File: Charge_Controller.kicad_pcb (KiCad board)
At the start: 2 copper layers, 127 x 73.7 mm, 147 parts, among them J1 SOLAR, J10 Conn_01x01_Female, J11 Conn_01x01_Female, J12 Conn_01x01_Female, J13 Conn_01x01_Female, J14 Conn_01x01_Female, J15 Conn_01x01_Female, J16 Conn_01x01_Female, J17 Conn_01x01_Female, J18 Conn_01x01_Female, J19 Conn_01x01_Female, J2 Conn_01x01_Female, J20 Conn_01x01_Female, J21 Conn_01x01_Female, J22 Conn_01x01_Female, J23 Conn_01x01_Female, J24 Conn_01x01_Female, J25 Conn_01x01_Female, J26 Conn_01x01_Female, J27 Conn_01x01_Female, J28 Conn_01x01_Female, J29 Conn_01x01_Female, J3 Conn_01x01_Female, J30 Conn_01x01_Female, J31 Conn_01x01_Female, J32 Conn_01x01_Female, J33 SOLAR, J34 BATT, J35 BATT, J36 FAN, J37 I2C_CON, J38 I2C_CON, J4 Conn_01x01_Female, J5 Conn_01x01_Female, J6 Conn_01x01_Female, J7 Conn_01x01_Female, J8 BATT, J9 USB_OTG, Q1 CSD19505, Q2 CSD19505, Q3 CSD19505, Q4 Si2306, Q5 2N3904, Q6 2N3904, Q7 PMOS-100V-78A, Q8 PMOS-100V-78A, Q9 Si2306, SW1 RIGHT, SW2 RIGHT, SW3 RIGHT, SW4 RIGHT, U1 ACS712-30A, U10 ADS1015, U11 NUP4202, U2 B1212, U3 AMS1117-5.0, U4 AMS1117-3.3, U5 XL7005A, U6 XL7005A, U7 IR2104, U8 ESP32-WROOM-32, U9 CH340G

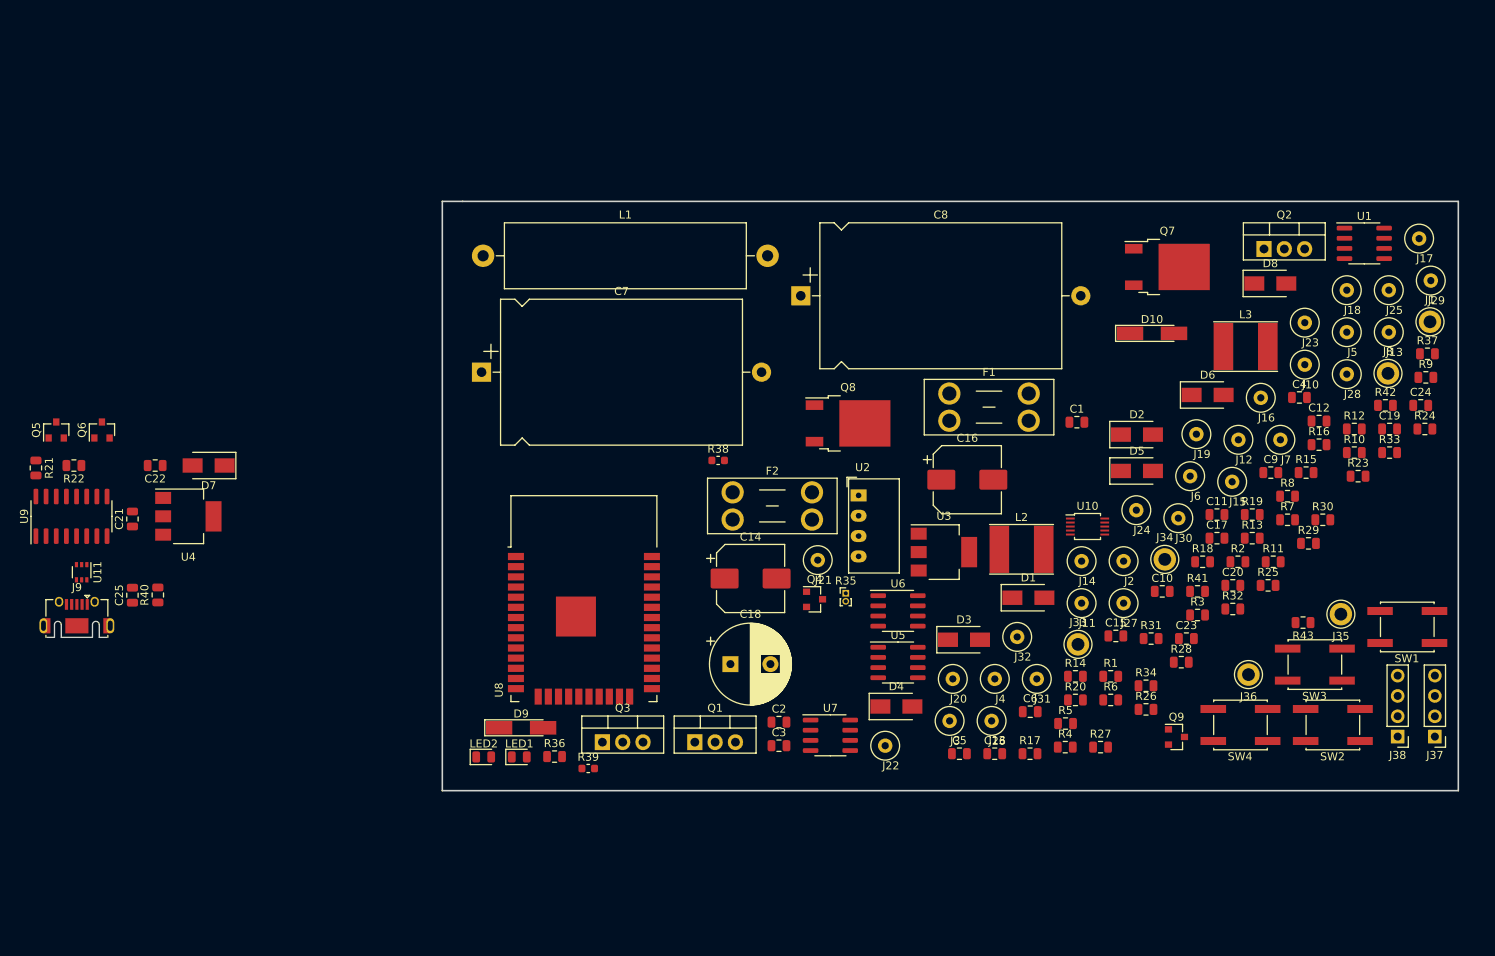
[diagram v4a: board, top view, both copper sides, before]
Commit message: Initial draft layout, no traces yet, but parts are mostly arranged.
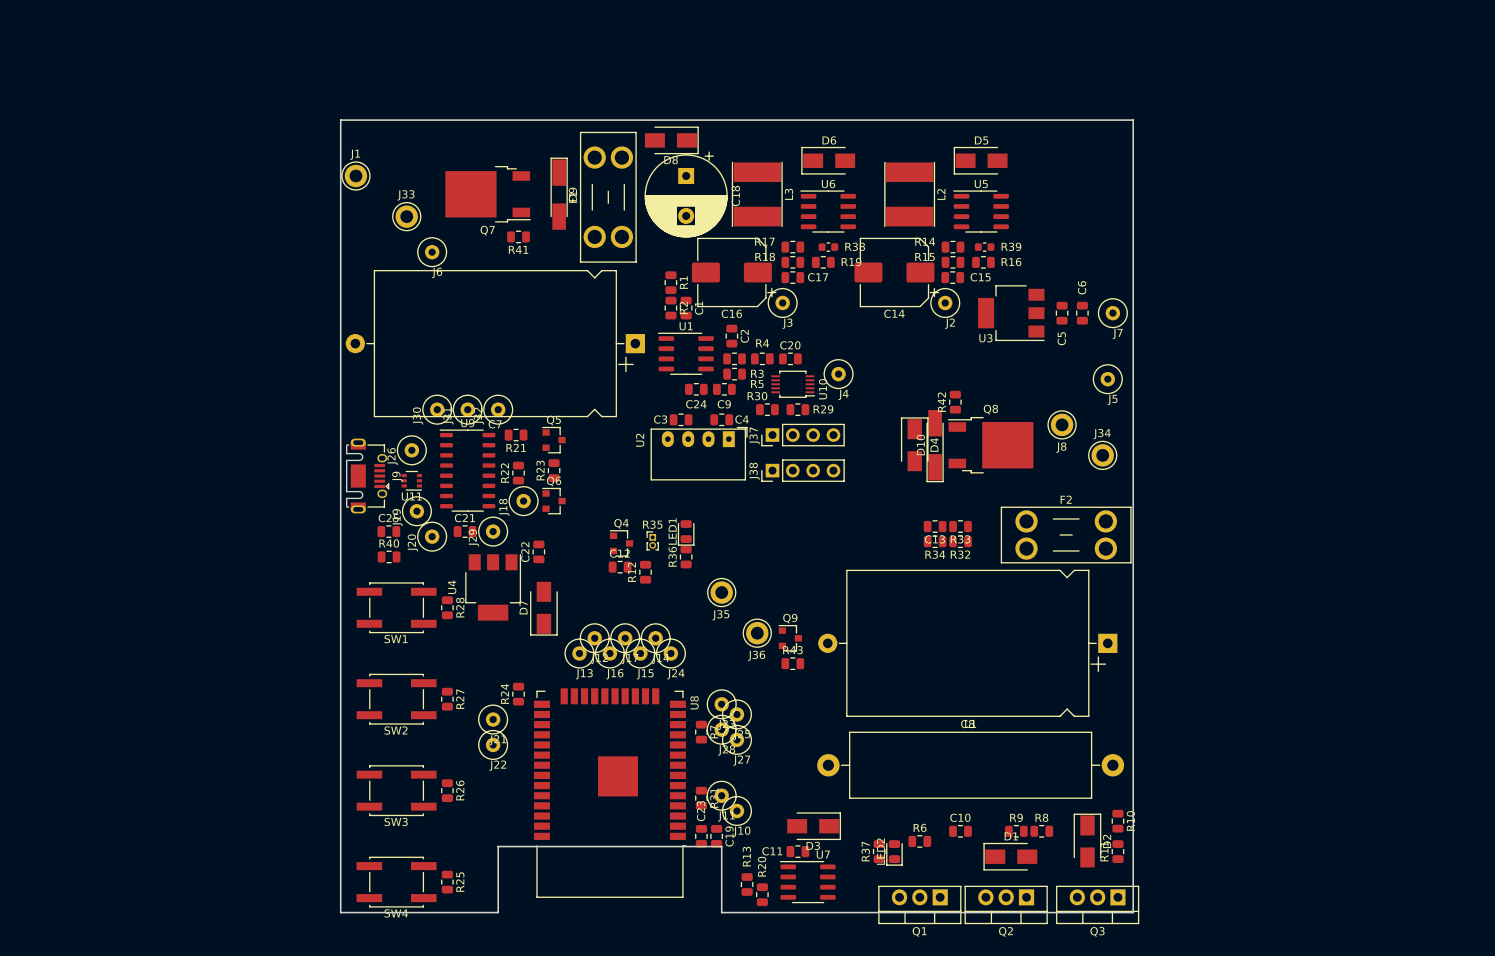
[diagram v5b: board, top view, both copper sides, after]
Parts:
- SW2: value RIGHT -> LEFT
- SW3: value RIGHT -> BACK
- SW4: value RIGHT -> SELECT
- U9: value CH340G -> CH340C; footprint Package_SO:SOIC-16_3.9x9.9mm_P1.27mm -> Package_SO:STC_SOP-16_3.9x9.9mm_P1.27mm
- moved J1 135.5 mm to (67.1, 58.7)
- moved SW1 126.4 mm to (72.2, 112.7)
- moved J29 121.3 mm to (84.2, 103.2), turned to 270 degrees
- moved R24 118.0 mm to (87.4, 123.5), turned to 90 degrees
- moved SW2 117.1 mm to (72.2, 124.1)
- moved SW3 115.9 mm to (72.2, 135.6)
- moved J17 111.1 mm to (100.7, 116.5)
- moved R25 109.1 mm to (78.5, 147.0), turned to 270 degrees
- moved J13 108.8 mm to (95.0, 118.4)
- moved SW4 107.3 mm to (72.2, 147.0)
- moved J18 106.2 mm to (88.0, 99.4), turned to 270 degrees
- moved R23 100.5 mm to (91.8, 95.6), turned to 90 degrees
- moved J33 99.5 mm to (73.4, 63.8)
- moved J6 98.8 mm to (76.6, 68.2)
- moved C19 98.3 mm to (112.2, 141.3), turned to 270 degrees
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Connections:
- SW4 pad 2: Net-(SW4-Pad2) -> +3V3
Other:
- board size 127 x 73.7 mm -> 99.1 x 99.1 mm

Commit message: More PCB initial setup, 2oz copper, widths, via's etc.
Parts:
- moved J9 0.75 mm to (68.1, 96.2)
- turned J1 to 90 degrees
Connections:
- net Net-(C10-Pad2) renamed /BuckFB
- net Net-(C18-Pad1) renamed /S+B+1A
- net Net-(C3-Pad2) renamed /S+Fused2
- net Net-(C7-Pad1) renamed /S+Fused
- net Net-(C8-Pad1) renamed /B+Fused
- net Net-(D10-Pad1) renamed /B+Polarity
- net Net-(D8-Pad2) renamed /S+Polarity
- net Net-(J1-Pad1) renamed /S+
- net Net-(J8-Pad1) renamed /B+
- net Net-(Q1-Pad2) renamed /S+Fused3
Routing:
- net /S+: track 0.00 -> 23.5 mm, vias 0 -> 1
- net GND: track 0.00 -> 3.30 mm, vias 0 -> 1
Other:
- outline, holes or cut-outs redrawn
- net class 1.00A_EXTERNAL_1oz_0.041ohm/in removed
- net class 1.6A_100V_EXTERNAL_2OZ added: clearance 0.254, trace_width 0.3048, via_dia 0.4, via_drill 0.2
- net class 15A_100V_EXTERNAL_2oz added: clearance 0.254, trace_width 6.4008, via_dia 7.300001, via_drill 6.3
- net class 3.44A_EXTERNAL_1oz_0.007ohm/in removed
- net class 30A_100V_EXTERNAL_2oz added: clearance 0.254, trace_width 16.6624, via_dia 7.300001, via_drill 6.3
- net class Default: clearance 0.2 -> 0.254; trace_width 0.2032 -> 0.3048; via_dia 0.6096 -> 0.4; via_drill 0.3048 -> 0.2
- rule trace_clearance: 0.2 -> 0.254
- rule trace_min: 0.2032 -> 0.2
- rule via_min_drill: 0.3 -> 0.2
- rule via_min_size: 0.2 -> 0.4

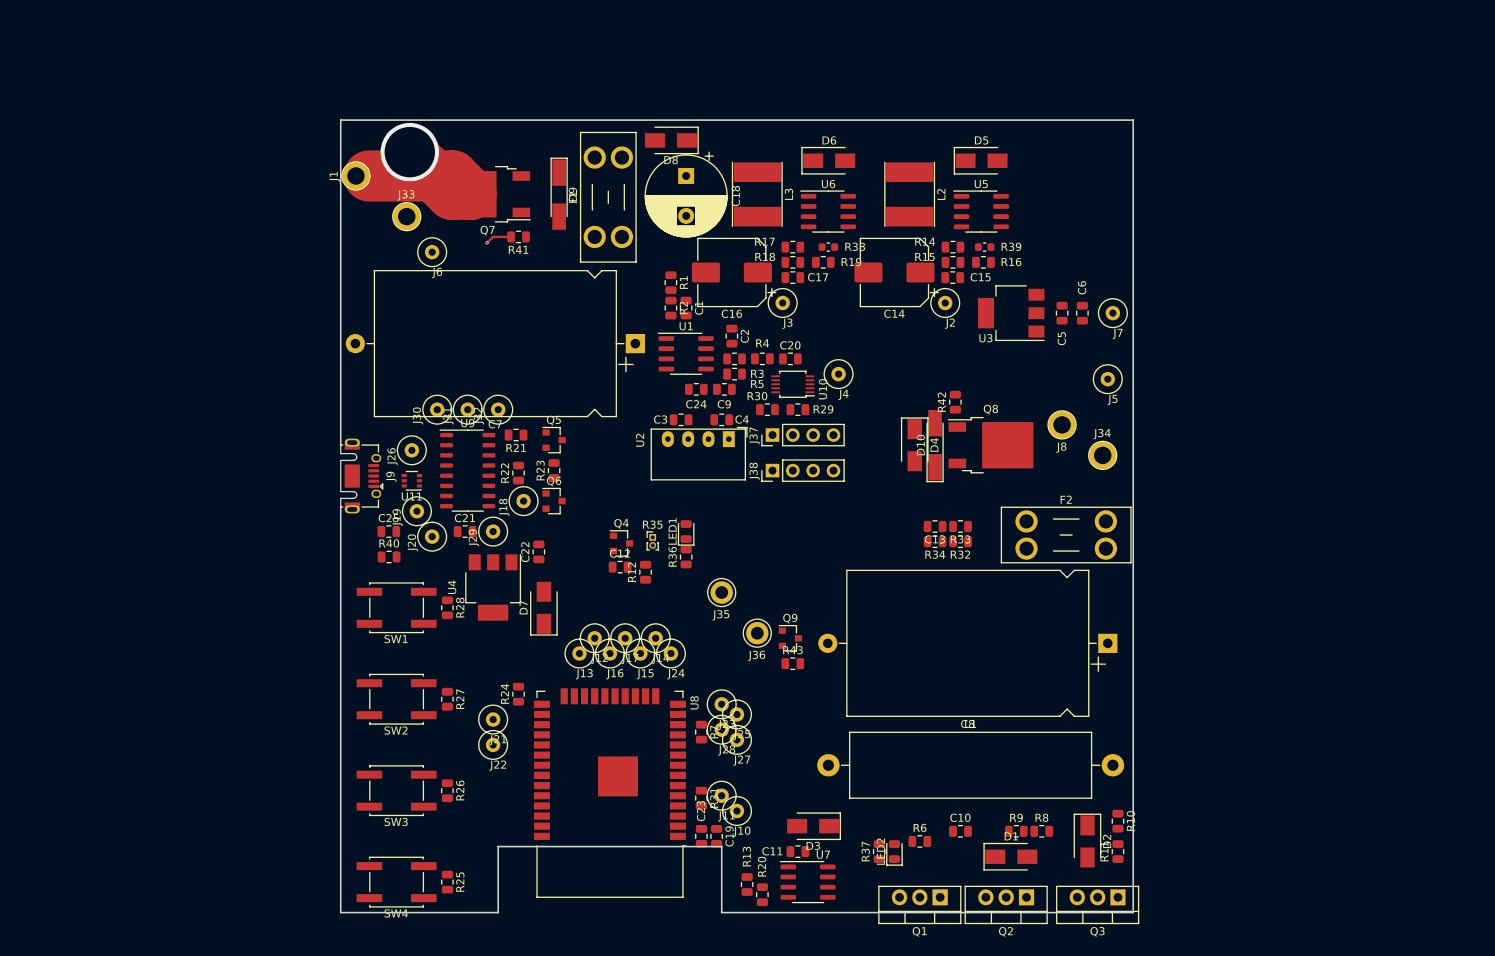
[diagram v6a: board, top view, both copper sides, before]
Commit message: Converted to KCAD 6, more draft layout.
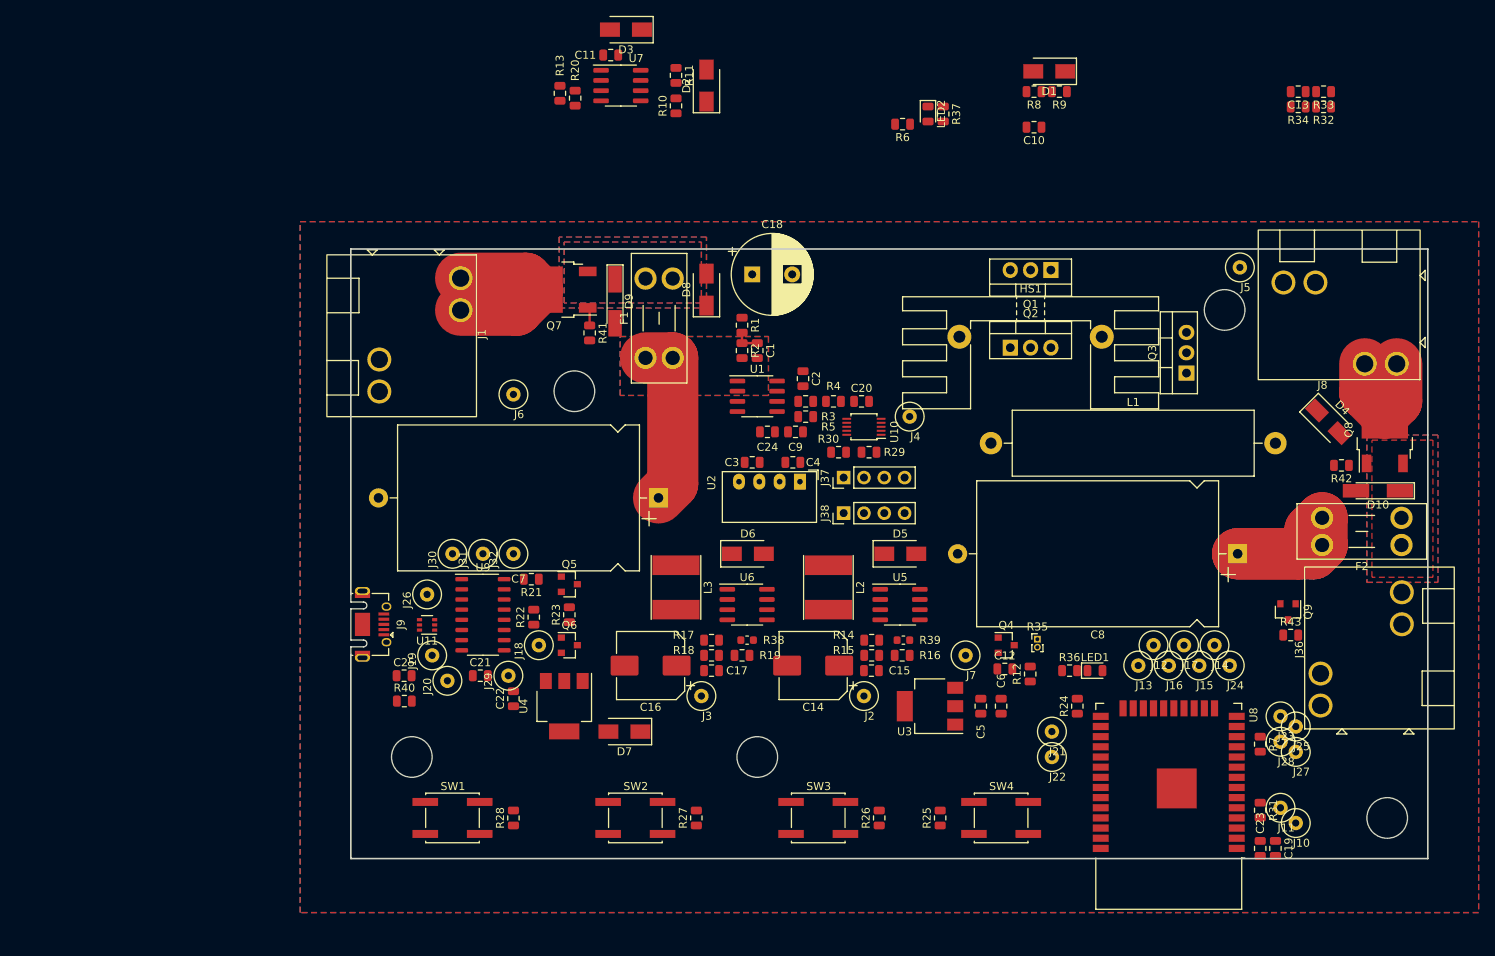
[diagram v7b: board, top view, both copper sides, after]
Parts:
- removed J33: SOLAR, TestPoint:TestPoint_Keystone_5005-5009_Compact
- removed J34, J35: BATT, TestPoint:TestPoint_Keystone_5005-5009_Compact
- added HS1: Heatsink, Heatsink:Heatsink_Stonecold_HS-132_32x14mm_2xFixation1.5mm, F.Cu at (151.4, 78.8)
- added LOGO1: Logo_Open_Hardware_Small, Symbol:OSHW-Symbol_6.7x6mm_SilkScreen, B.Cu at (194.1, 131.8)
- J1, J36, J8: footprint TestPoint:TestPoint_Keystone_5005-5009_Compact -> Phoenix_10.16_terminal_1709681:Phoenix_10.16_terminal_1709681
- moved R11 111.7 mm to (107.1, 46.2), turned to -90 degrees
- moved D2 105.8 mm to (110.9, 47.4), turned to 90 degrees
- moved R10 105.1 mm to (107.1, 50.0), turned to 90 degrees
- moved C11 102.3 mm to (98.9, 43.6)
- moved U7 102.3 mm to (100.2, 47.4)
- moved D3 102.3 mm to (100.8, 40.4)
- moved R20 102.3 mm to (94.5, 49.0)
- moved R13 101.6 mm to (92.6, 48.4)
- moved D1 98.3 mm to (153.7, 45.6), turned to 180 degrees
- moved R9 92.6 mm to (155.0, 48.2), turned to 180 degrees
- moved R37 92.5 mm to (140.5, 51.0), turned to -90 degrees
- moved R8 92.5 mm to (151.8, 48.2), turned to 180 degrees
- moved LED2 92.3 mm to (138.6, 51.0), turned to -90 degrees
- moved R6 89.7 mm to (135.4, 52.2), turned to 180 degrees
- moved C10 88.5 mm to (151.8, 52.6), turned to 180 degrees
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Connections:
- net +3V3 renamed +3.3VA
- J36 pad 1: Net-(J36-Pad1) -> /12V
- Q9 pad 1: Net-(J36-Pad1) -> Net-(J36-Pad2)
- U8 pad 32: (no net) -> unconnected-(U8-Pad32)
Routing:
- net /B+Fused: track 0.00 -> 39.9 mm
- net /S+Fused: track 0.00 -> 21.6 mm
- net /B+: track 0.00 -> 14.0 mm
- net GND: track 3.30 -> 0.00 mm, vias 1 -> 0
- net /A3: track 0.00 -> 3.20 mm
- net /S+: track 23.5 -> 20.8 mm, vias 1 -> 0
- net Net-(D9-Pad2): track 0.00 -> 2.30 mm
- added copper zone on F.Cu, net /B+Polarity
- added copper zone on B.Cu, net /S+Fused
- added copper zone on F.Cu, net /S+Fused
- added copper zone on B.Cu, net /S+Polarity
- added copper zone on F.Cu, net /S+Polarity
- added copper zone on B.Cu, net GND
- added copper zone on F.Cu, net GND
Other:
- board size 99.1 x 99.1 mm -> 134.6 x 76.2 mm
- net class 1.6A_100V_EXTERNAL_2OZ removed
- net class 15A_100V_EXTERNAL_2oz removed
- net class 30A_100V_EXTERNAL_2oz removed
- net class Default removed

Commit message: Another incremental layout draft.
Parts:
- R35: footprint Connector_PinHeader_1.00mm:PinHeader_1x02_P1.00mm_Vertical -> Connector_PinHeader_2.54mm:PinHeader_1x02_P2.54mm_Vertical
- moved R13 92.9 mm to (173.8, 93.7)
- moved R20 89.7 mm to (171.9, 94.3)
- moved R11 85.4 mm to (181.9, 87.3), turned to 0 degrees
- moved C11 82.3 mm to (164.2, 93.7), turned to -90 degrees
- moved U7 81.4 mm to (168.1, 92.4), turned to 0 degrees
- moved R10 79.5 mm to (177.8, 86.3)
- moved D3 79.1 mm to (161.1, 91.7), turned to -90 degrees
- moved D2 75.1 mm to (175.2, 86.3)
- moved C13 67.2 mm to (144.6, 101.9), turned to -90 degrees
- moved R33 66.7 mm to (144.6, 98.7), turned to -90 degrees
- moved R34 64.5 mm to (146.5, 101.9), turned to -90 degrees
- moved R32 64.0 mm to (146.5, 98.7), turned to -90 degrees
- moved R8 43.2 mm to (143.0, 90.5), turned to 0 degrees
- moved C10 40.7 mm to (143.0, 92.4), turned to 0 degrees
- moved D1 40.4 mm to (146.5, 85.4), turned to 90 degrees
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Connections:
- U11 pad 1: /USBV -> /USBID
- U11 pad 3: /USBID -> Net-(J9-Pad3)
- U11 pad 4: Net-(J9-Pad3) -> Net-(J9-Pad2)
- U11 pad 6: Net-(J9-Pad2) -> /USBV
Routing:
- net +3.3VA: track 0.00 -> 319.2 mm, vias 0 -> 7
- net /EN: track 0.00 -> 179.3 mm, vias 0 -> 2
- net /S+B+1A: track 0.00 -> 172.7 mm
- net /12V: track 0.00 -> 156.1 mm, vias 0 -> 6
- net /5.0V: track 0.00 -> 134.4 mm, vias 0 -> 4
- net GND: track 0.00 -> 127.8 mm, vias 0 -> 89
- net /USBID: track 0.00 -> 125.0 mm, vias 0 -> 5
- net /RX: track 0.00 -> 108.2 mm, vias 0 -> 6
- net /TX: track 0.00 -> 106.8 mm, vias 0 -> 6
- net Net-(C3-Pad1): track 0.00 -> 105.2 mm
- net /GPIO34: track 0.00 -> 98.1 mm
- net /PB-RHT: track 0.00 -> 93.0 mm
- net /GPIO0: track 0.00 -> 78.8 mm, vias 0 -> 2
- net /SCL: track 0.00 -> 74.3 mm
- net /SDA: track 0.00 -> 72.7 mm
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- added copper zone on B.Cu, net /B+Fused
- added copper zone on F.Cu, net /B+Fused
- added copper zone on B.Cu, net /BuckFB
- added copper zone on F.Cu, net /BuckFB
- added copper zone on B.Cu, net /S+Fused2
- added copper zone on F.Cu, net /S+Fused2
- added copper zone on B.Cu, net /S+Fused3
- added copper zone on F.Cu, net /S+Fused3
